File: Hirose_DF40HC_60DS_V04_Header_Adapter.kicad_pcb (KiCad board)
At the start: 2 copper layers, 30 x 86 mm, 2 parts, among them J1 DF40HC_4.0_-60DS-0.4V_51_, J2 Conn_02x30_Odd_Even

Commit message: Update degsign after gerbers generation
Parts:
- added H1: MountingHole, MountingHole:MountingHole_3.2mm_M3, F.Cu at (121.9, 37.6)
- added H2: MountingHole, MountingHole:MountingHole_3.2mm_M3, F.Cu at (121.9, 113.5)
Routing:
- added copper zone on B.Cu, net (none)
- added copper zone on F.Cu, net (none)
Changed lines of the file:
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@@
     (tracks 453)
     (zones 0)
-    (modules 2)
+    (modules 4)
     (nets 61)
   )
@@
     (visible_elements FFFFFF7F)
     (pcbplotparams
-      (layerselection 0x010fc_ffffffff)
+      (layerselection 0x010f0_ffffffff)
       (usegerberextensions false)
       (usegerberattributes true)
@@
       (outputformat 1)
       (mirror false)
-      (drillshape 1)
+      (drillshape 0)
       (scaleselection 1)
-      (outputdirectory ""))
+      (outputdirectory "prod/V1A/"))
   )
   (net 0 "")
@@
     (add_net "Net-(J1-Pad60)")
     (add_net "Net-(J1-Pad8)")
+  )
+  (module MountingHole:MountingHole_3.2mm_M3 (layer F.Cu)
+    (at 121.92 113.538)
+    (descr "Mounting Hole 3.2mm, no annular, M3")
+    (tags "mounting hole 3.2mm no annular m3")
+    (attr virtual)
+    (fp_text reference H2 (at 0 -4.2) (layer F.SilkS)
+      (effects (font (size 1 1) (thickness 0.15)))
+    )
+    (fp_text value MountingHole (at 0 4.2) (layer F.Fab)
+      (effects (font (size 1 1) (thickness 0.15)))
+    )
+    (fp_text user %R (at 0.3 0) (layer F.Fab)
+      (effects (font (size 1 1) (thickness 0.15)))
+    )
+    (fp_circle (center 0 0) (end 3.2 0) (layer Cmts.User) (width 0.15))
+    (fp_circle (center 0 0) (end 3.45 0) (layer F.CrtYd) (width 0.05))
+    (pad 1 np_thru_hole circle (at 0 0) (size 3.2 3.2) (drill 3.2) (layers *.Cu *.Mask))
+  )
+  (module MountingHole:MountingHole_3.2mm_M3 (layer F.Cu)
+    (at 121.92 37.592 180)
+    (descr "Mounting Hole 3.2mm, no annular, M3")
+    (tags "mounting hole 3.2mm no annular m3")
+    (attr virtual)
+    (fp_text reference H1 (at 0 -4.2) (layer F.SilkS)
+      (effects (font (size 1 1) (thickness 0.15)))
+    )
+    (fp_text value MountingHole (at 0 4.2) (layer F.Fab)
+      (effects (font (size 1 1) (thickness 0.15)))
+    )
+    (fp_text user %R (at 0.3 0) (layer F.Fab)
+      (effects (font (size 1 1) (thickness 0.15)))
+    )
+    (fp_circle (center 0 0) (end 3.2 0) (layer Cmts.User) (width 0.15))
+    (fp_circle (center 0 0) (end 3.45 0) (layer F.CrtYd) (width 0.05))
+    (pad 1 np_thru_hole circle (at 0 0 180) (size 3.2 3.2) (drill 3.2) (layers *.Cu *.Mask))
   )
   (module footprints:DF40HC4060DS04V51 (layer F.Cu)
@@
   (segment (start 116.128 69.9) (end 110.49 64.262) (width 0.18) (layer F.Cu) (net 60))
   (segment (start 116.31 69.9) (end 116.128 69.9) (width 0.18) (layer F.Cu) (net 60))
+  (zone (net 0) (net_name "") (layer F.Cu) (hatch edge 0.508)
+    (connect_pads (clearance 0.508))
+    (min_thickness 0.254)
+    (fill yes (arc_segments 32) (thermal_gap 0.508) (thermal_bridge_width 0.508))
+    (polygon
+      (pts
+        (xy 137.414 118.364) (xy 107.696 118.364) (xy 107.696 32.512) (xy 137.414 32.512)
+      )
+    )
+  )
+  (zone (net 0) (net_name "") (layer B.Cu) (hatch edge 0.508)
+    (connect_pads (clearance 0.508))
+    (min_thickness 0.254)
+    (fill yes (arc_segments 32) (thermal_gap 0.508) (thermal_bridge_width 0.508))
+    (polygon
+      (pts
+        (xy 137.414 118.364) (xy 107.696 118.364) (xy 107.696 32.512) (xy 137.414 32.512)
+      )
+    )
+  )
 )

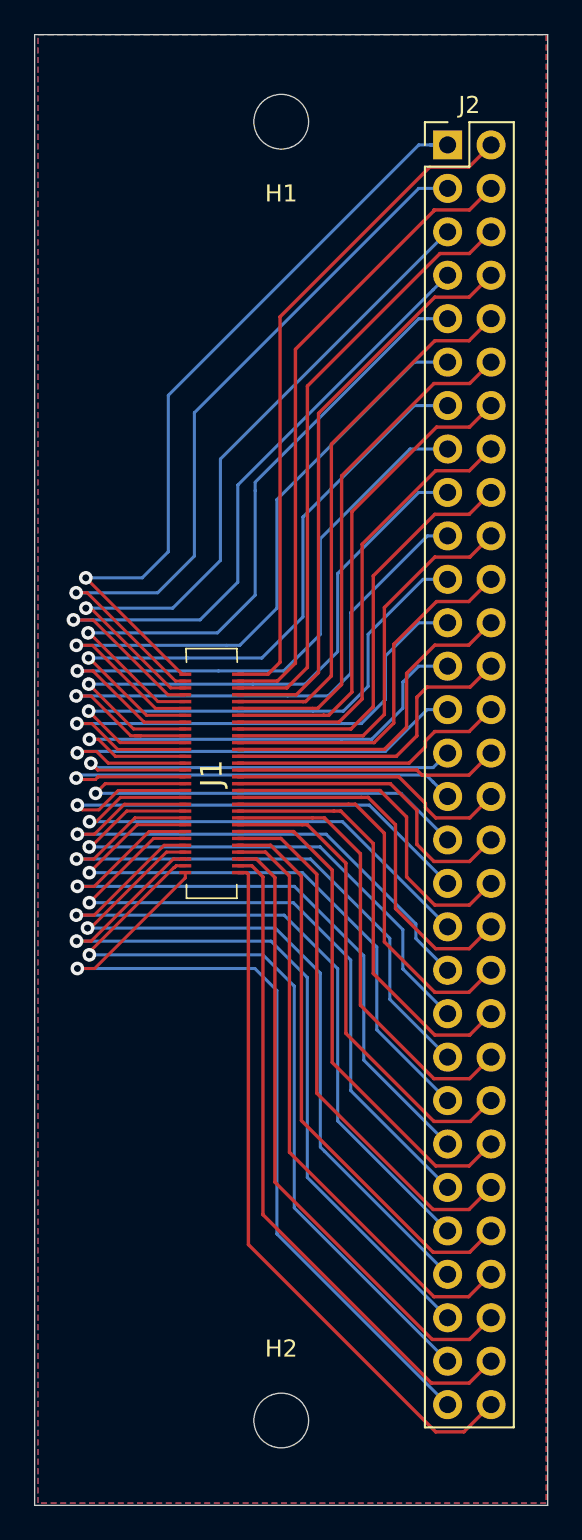
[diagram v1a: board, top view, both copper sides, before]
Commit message: Update footprints
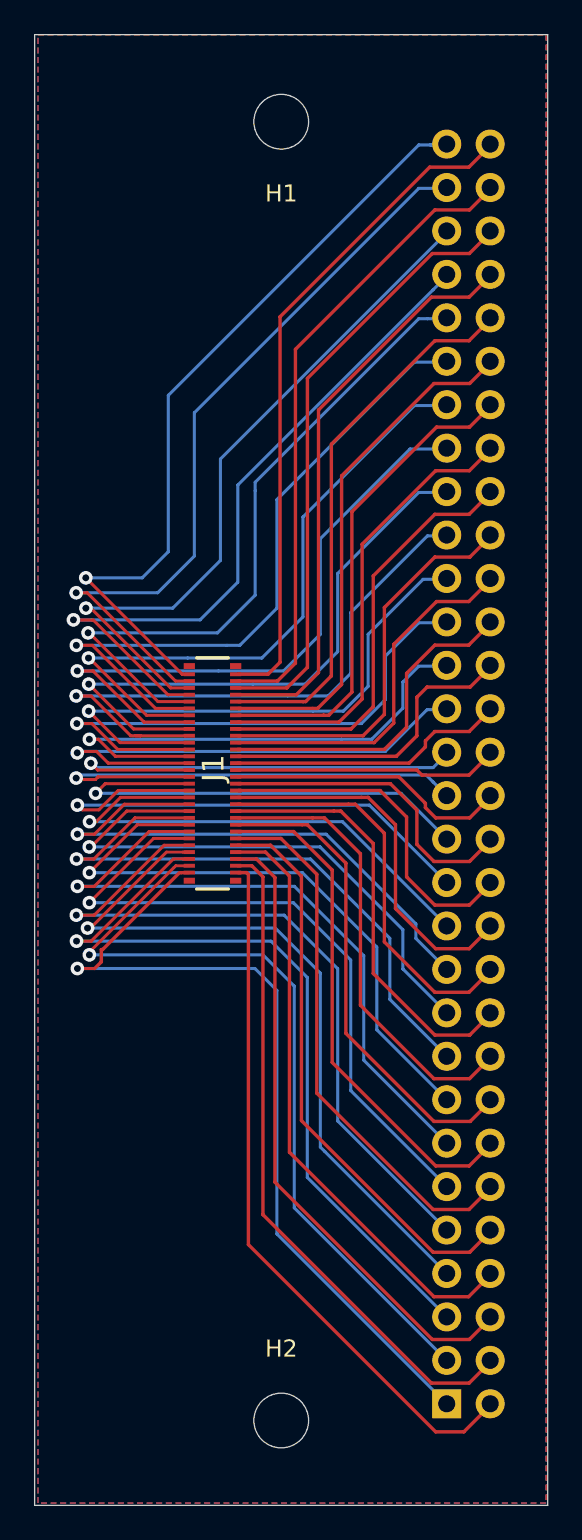
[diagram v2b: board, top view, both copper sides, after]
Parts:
- J1: footprint footprints:DF40HC4060DS04V51 -> footprints:DF40C-60DP-0.4V_51_
- J2: moved to B.Cu
- moved J2 73.6 mm to (131.6, 112.6)
- moved J1 0.05 mm to (117.9, 75.7)
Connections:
- J2 pad 1: /1 -> /59
- J2 pad 10: Net-(J1-Pad10) -> Net-(J1-Pad52)
- J2 pad 11: /11 -> /49
- J2 pad 12: Net-(J1-Pad12) -> Net-(J1-Pad50)
- J2 pad 13: /13 -> /47
- J2 pad 14: Net-(J1-Pad14) -> Net-(J1-Pad48)
- J2 pad 15: /15 -> /45
- J2 pad 16: Net-(J1-Pad16) -> Net-(J1-Pad46)
- J2 pad 17: /17 -> /43
- J2 pad 18: Net-(J1-Pad18) -> Net-(J1-Pad44)
- J2 pad 19: /19 -> /41
- J2 pad 2: Net-(J1-Pad2) -> Net-(J1-Pad60)
- J2 pad 20: Net-(J1-Pad20) -> Net-(J1-Pad42)
- J2 pad 21: /21 -> /39
- J2 pad 22: Net-(J1-Pad22) -> Net-(J1-Pad40)
- J2 pad 23: /23 -> /37
- J2 pad 24: Net-(J1-Pad24) -> Net-(J1-Pad38)
- J2 pad 25: /25 -> /35
- J2 pad 26: Net-(J1-Pad26) -> Net-(J1-Pad36)
- J2 pad 27: /27 -> /33
- J2 pad 28: Net-(J1-Pad28) -> Net-(J1-Pad34)
- J2 pad 29: /29 -> /31
- J2 pad 3: /3 -> /57
- J2 pad 30: Net-(J1-Pad30) -> Net-(J1-Pad32)
- J2 pad 31: /31 -> /29
- J2 pad 32: Net-(J1-Pad32) -> Net-(J1-Pad30)
- J2 pad 33: /33 -> /27
- J2 pad 34: Net-(J1-Pad34) -> Net-(J1-Pad28)
- J2 pad 35: /35 -> /25
- J2 pad 36: Net-(J1-Pad36) -> Net-(J1-Pad26)
- J2 pad 37: /37 -> /23
- J2 pad 38: Net-(J1-Pad38) -> Net-(J1-Pad24)
- J2 pad 39: /39 -> /21
- J2 pad 4: Net-(J1-Pad4) -> Net-(J1-Pad58)
- J2 pad 40: Net-(J1-Pad40) -> Net-(J1-Pad22)
- J2 pad 41: /41 -> /19
- J2 pad 42: Net-(J1-Pad42) -> Net-(J1-Pad20)
- J2 pad 43: /43 -> /17
- J2 pad 44: Net-(J1-Pad44) -> Net-(J1-Pad18)
- J2 pad 45: /45 -> /15
- J2 pad 46: Net-(J1-Pad46) -> Net-(J1-Pad16)
- J2 pad 47: /47 -> /13
- J2 pad 48: Net-(J1-Pad48) -> Net-(J1-Pad14)
- J2 pad 49: /49 -> /11
- J2 pad 5: /5 -> /55
- J2 pad 50: Net-(J1-Pad50) -> Net-(J1-Pad12)
- J2 pad 51: /51 -> /9
- J2 pad 52: Net-(J1-Pad52) -> Net-(J1-Pad10)
- J2 pad 53: /53 -> /7
- J2 pad 54: Net-(J1-Pad54) -> Net-(J1-Pad8)
- J2 pad 55: /55 -> /5
- J2 pad 56: Net-(J1-Pad56) -> Net-(J1-Pad6)
- J2 pad 57: /57 -> /3
- J2 pad 58: Net-(J1-Pad58) -> Net-(J1-Pad4)
- J2 pad 59: /59 -> /1
- J2 pad 6: Net-(J1-Pad6) -> Net-(J1-Pad56)
- J2 pad 60: Net-(J1-Pad60) -> Net-(J1-Pad2)
- J2 pad 7: /7 -> /53
- J2 pad 8: Net-(J1-Pad8) -> Net-(J1-Pad54)
- J2 pad 9: /9 -> /51
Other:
- rule trace_min: 0.18 -> 0.16
